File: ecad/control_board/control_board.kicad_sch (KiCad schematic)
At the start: 31 parts, among them J1 USB_C_Receptacle_USB2.0_16P, J2 JST SH, U1 W25Q16JVUXIQ, U2 NCP1117-3.3_SOT223, U3 RP2040, Y1 ABM8-272-T3

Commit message: [WIP]
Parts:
- removed U2: NCP1117-3.3_SOT223, Package_TO_SOT_SMD:SOT-223-3_TabPin2, symbol Regulator_Linear:NCP1117-3.3_SOT223
- added C17, C18: 100n, Capacitor_SMD:C_0402_1005Metric, symbol Device:C
- added J3, J4, J5: JST SH, Connector_JST:JST_SH_BM04B-SRSS-TB_1x04-1MP_P1.00mm_Vertical, symbol Connector_Generic:Conn_01x04
- added R10, R11, R8, R9: 5.1k, Resistor_SMD:R_0402_1005Metric, symbol Device:R
- added U2: TLV75733PDBV, Package_TO_SOT_SMD:SOT-23-5, symbol Regulator_Linear:TLV75733PDBV
- added U4: TCA9406DCTR, Package_SO:SSOP-8_2.95x2.8mm_P0.65mm, symbol Interface:TCA9406DC
- C4, C5: value 10u -> 2u2; footprint Capacitor_SMD:C_0805_2012Metric -> Capacitor_SMD:C_0402_1005Metric
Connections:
- net +3V3: now also C17.1, C18.1, J3.1 (Pin_1), J4.1 (Pin_1), J5.1 (Pin_1), R10.1, R11.1, R8.1, R9.1, U2.5 (OUT), U4.3 (VCCA), U4.7 (VCCB)
- net +5V: now also U2.1 (IN), U2.3 (EN)
- net GND: now also C17.2, C18.2, J3.4 (Pin_4), J4.4 (Pin_4), J5.4 (Pin_4), U2.2 (GND), U4.2 (GND)
- new net PICO/KEY/SCL: R8.2, U4.5 (SCL_A)
- new net PICO/KEY/SDA: R9.2, U4.4 (SDA_A)
- new net TOP/SCL: J3.3 (Pin_3), J4.3 (Pin_3), J5.3 (Pin_3), R10.2, U4.8 (SCL_B)
- new net TOP/SDA: J3.2 (Pin_2), J4.2 (Pin_2), J5.2 (Pin_2), R11.2, U4.1 (SDA_B)
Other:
- note added: "3V3 @ 1A LDO"
- note added: "Flash Memory"
- note added: "PUSH BUTTONS"
- note added: "USB Type C 2.0 RCPT"
- note added: "XTAL"
- moved on the sheet: BOOTSEL1, C1, C10, C11, C12, C13, C14, C15, C16, C2, C3, C4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

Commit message: Makes a control_board
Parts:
- added C19, C20, C21, C22: 100n, Capacitor_SMD:C_0402_1005Metric, symbol Device:C
- added J10, J11, J3, J4, J5, J9: JST SH 4, woodpecker:JST_SH_BM04B-SRSS-TB_1x04-1MP_P1.00mm_Vertical, symbol Connector_Generic:Conn_01x04
- added J12: JST PH 4, woodpecker:JST_PH_B4B-PH-SM4-TB_1x04-1MP_P2.00mm_Vertical, symbol Connector_Generic:Conn_01x04
- added J13, J14: JST PH 3, woodpecker:JST_PH_B3B-PH-SM4-TB_1x03-1MP_P2.00mm_Vertical, symbol Connector_Generic:Conn_01x03
- added R12, R13, R16, R17: 2.2k, Resistor_SMD:R_0402_1005Metric, symbol Device:R
- added R18, R19: 5.1k, Resistor_SMD:R_0402_1005Metric, symbol Device:R
- added U5, U6: TCA9406DCTR, Package_SO:SSOP-8_2.95x2.8mm_P0.65mm, symbol Interface:TCA9406DC
- J2: value JST SH -> JST SH 3; footprint Connector_JST:JST_SH_BM03B-SRSS-TB_1x03-1MP_P1.00mm_Vertical -> woodpecker:JST_SH_BM03B-SRSS-TB_1x03-1MP_P1.00mm_Vertical
- J6: renamed from J5; value JST SH -> JST SH 4; footprint Connector_JST:JST_SH_BM04B-SRSS-TB_1x04-1MP_P1.00mm_Vertical -> woodpecker:JST_SH_BM04B-SRSS-TB_1x04-1MP_P1.00mm_Vertical
- J7: renamed from J3; value JST SH -> JST SH 4; footprint Connector_JST:JST_SH_BM04B-SRSS-TB_1x04-1MP_P1.00mm_Vertical -> woodpecker:JST_SH_BM04B-SRSS-TB_1x04-1MP_P1.00mm_Vertical
- J8: renamed from J4; value JST SH -> JST SH 4; footprint Connector_JST:JST_SH_BM04B-SRSS-TB_1x04-1MP_P1.00mm_Vertical -> woodpecker:JST_SH_BM04B-SRSS-TB_1x04-1MP_P1.00mm_Vertical
- R10, R11: value 5.1k -> 2.2k
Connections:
- net PICO/KEY/SCL is gone; now on net I2C0/SCL: R8.2, U4.5 (SCL_A)
- net PICO/KEY/SDA is gone; now on net I2C0/SDA: R9.2, U4.4 (SDA_A)
- net +3V3: now also C19.1, C20.1, C21.1, C22.1, J10.1 (Pin_1), J11.1 (Pin_1), J3.1 (Pin_1), J4.1 (Pin_1), J5.1 (Pin_1), J9.1 (Pin_1), R12.1, R13.1, R16.1, R17.1, R18.1, R19.1, U5.3 (VCCA), U5.7 (VCCB), U6.3 (VCCA), U6.7 (VCCB)
- net +5V: now also J12.4 (Pin_4), J13.3 (Pin_3), J14.3 (Pin_3)
- net GND: now also C19.2, C20.2, C21.2, C22.2, J10.4 (Pin_4), J11.4 (Pin_4), J12.1 (Pin_1), J13.1 (Pin_1), J14.1 (Pin_1), J3.4 (Pin_4), J4.4 (Pin_4), J5.4 (Pin_4), J9.4 (Pin_4), U5.2 (GND), U6.2 (GND)
- net I2C0/SCL: now reaches U3.12 (GPIO9)
- net I2C0/SCL: now also U5.5 (SCL_A)
- net I2C0/SDA: now reaches U3.15 (GPIO12)
- net I2C0/SDA: now also U5.4 (SDA_A)
- net I2C_E: now reaches U3.2 (GPIO0)
- net I2C_E: now also U4.6 (OE), U5.6 (OE), U6.6 (OE)
- net BOT/DOUT: now reaches U3.30 (GPIO19)
- net BOT/DOUT: now also J14.2 (Pin_2)
- net MID/DOUT: now reaches U3.31 (GPIO20)
- net MID/DOUT: now also J13.2 (Pin_2)
- net TOP/DOUT: now reaches U3.39 (GPIO27_ADC1)
- net TOP/DOUT: now also J12.3 (Pin_3)
- net TOP/SDOUT: now reaches U3.40 (GPIO28_ADC2)
- net TOP/SDOUT: now also J12.2 (Pin_2)
- net I2C1/SCL: now reaches U3.5 (GPIO3)
- net I2C1/SCL: now also R18.2, U6.5 (SCL_A)
- net I2C1/SDA: now reaches U3.8 (GPIO6)
- net I2C1/SDA: now also R19.2, U6.4 (SDA_A)
- new net BOT/SCL: J10.3 (Pin_3), J11.3 (Pin_3), J9.3 (Pin_3), R12.2, U5.8 (SCL_B)
- new net BOT/SDA: J10.2 (Pin_2), J11.2 (Pin_2), J9.2 (Pin_2), R13.2, U5.1 (SDA_B)
- new net MID/SCL: J3.3 (Pin_3), J4.3 (Pin_3), J5.3 (Pin_3), R16.2, U6.8 (SCL_B)
- new net MID/SDA: J3.2 (Pin_2), J4.2 (Pin_2), J5.2 (Pin_2), R17.2, U6.1 (SDA_B)
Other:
- note added: "I2C Buffer Bot"
- note added: "I2C Buffer Mid"
- note added: "I2C Buffer Top"
- note added: "SWD"
- moved on the sheet: C10, C11, C12, C13, C14, C15, C16, C17, C18, C6, C7, C8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

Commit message: [WIP] Control board
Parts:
- removed C18, C19, C20, C21, C22: 100n, Capacitor_SMD:C_0402_1005Metric, symbol Device:C
- removed J10, J11, J3, J4, J5, J6, J7, J8, J9: JST SH 4, woodpecker:JST_SH_BM04B-SRSS-TB_1x04-1MP_P1.00mm_Vertical, symbol Connector_Generic:Conn_01x04
- removed J12: JST PH 4, woodpecker:JST_PH_B4B-PH-SM4-TB_1x04-1MP_P2.00mm_Vertical, symbol Connector_Generic:Conn_01x04
- removed J13, J14: JST PH 3, woodpecker:JST_PH_B3B-PH-SM4-TB_1x03-1MP_P2.00mm_Vertical, symbol Connector_Generic:Conn_01x03
- removed R10, R11, R12, R13, R16, R17: 2.2k, Resistor_SMD:R_0402_1005Metric, symbol Device:R
- removed R18, R19, R4, R8, R9: 5.1k, Resistor_SMD:R_0402_1005Metric, symbol Device:R
- removed R7: 200, Resistor_SMD:R_0402_1005Metric, symbol Device:R
- removed U4, U5, U6: TCA9406DCTR, Package_SO:SSOP-8_2.95x2.8mm_P0.65mm, symbol Interface:TCA9406DC
- added D1: 1N4148WS, Diode_SMD:D_SOD-323, symbol Diode:1N4148WS
- added FB1: FerriteBead, symbol Device:FerriteBead
- added U4: TUSB320I, Package_DFN_QFN:Texas_X2QFN-12_1.6x1.6mm_P0.4mm, symbol Interface_USB:TUSB320I
- C9: value 2u2 -> 1u; footprint Capacitor_SMD:C_0402_1005Metric -> (none)
- R3: value 5.1k -> 900k
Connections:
- net +3V3: no longer C17.1
- net +5V: no longer J1.A4 (VBUS), J1.A9 (VBUS), J1.B4 (VBUS), J1.B9 (VBUS)
- net CC1: now also U4.1 (CC1)
- net CC2: now also U4.2 (CC2); no longer R3.1
- net GND: now also U4.10 (GND), U4.11 (~{EN}), U4.3 (PORT); no longer R3.2
- net 3V3_ADC: no longer names the net of U3.43 (ADC_AVDD)
- net 3V3_ADC: no longer C9.1
- net BOT/DOUT: no longer names the net of U3.30 (GPIO19)
- net I2C0/SCL: no longer names the net of U3.12 (GPIO9)
- net I2C0/SDA: no longer names the net of U3.15 (GPIO12)
- net I2C1/SCL: no longer names the net of U3.5 (GPIO3)
- net I2C1/SDA: no longer names the net of U3.8 (GPIO6)
- net I2C_E: no longer names the net of U3.2 (GPIO0)
- net MID/DOUT: no longer names the net of U3.31 (GPIO20)
- net TOP/DOUT: no longer names the net of U3.39 (GPIO27_ADC1)
- net TOP/SDOUT: no longer names the net of U3.40 (GPIO28_ADC2)
- new net: R3.2, U4.4 (VBUS_DET)
- new net USB_OUT1: U4.7 (SDA/OUT1)
- new net USB_OUT2: U4.8 (SCL/OUT2)
- new net VBUS: D1.2 (A), FB1.2, R3.1
- new net VBUS_5V: C17.1, D1.1 (K), U4.12 (VDD)
- new net VBUS_UNFLT: C9.1, FB1.1, J1.A4 (VBUS), J1.A9 (VBUS), J1.B4 (VBUS), J1.B9 (VBUS)
- no-connect marks 2 -> 5
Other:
- note added: "USB CC Controller"
- note removed: "I2C Buffer Bot"
- note removed: "I2C Buffer Mid"
- note removed: "I2C Buffer Top"
- moved on the sheet: C10, C11, C12, C13, C14, C15, C16, C3, C4, C5, C6, C7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

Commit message: [WIP] control board
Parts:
- added C18, C19: 100n, Capacitor_SMD:C_0402_1005Metric, symbol Device:C
- added J10, J9: JST PH 3, woodpecker:JST_PH_S3B-PH-SM4-TB_1x03-1MP_P2.00mm_Horizontal, symbol Connector_Generic:Conn_01x03
- added J3, J4, J5, J6, J7, J8: JST SH 3, woodpecker:JST_SH_BM03B-SRSS-TB_1x03-1MP_P1.00mm_Vertical, symbol Connector_Generic:Conn_01x03
- added Q6: RE1C002UN, Package_TO_SOT_SMD:SOT-416, symbol Device:Q_NMOS_GSD
- added R4: 71k5, Resistor_SMD:R_0402_1005Metric, symbol Device:R
- added R7, R8: 27k, Resistor_SMD:R_0402_1005Metric, symbol Device:R
- added U5: TPS2552DRV, woodpecker:Texas_WSON-6-1EP_2x2mm_P0.65mm_EP1x1.6mm_ThermalVias, symbol woodpecker:TPS2552DRV
- J2: footprint woodpecker:JST_SH_BM03B-SRSS-TB_1x03-1MP_P1.00mm_Vertical -> woodpecker:JST_SH_SM03B-SRSS-TB_1x03-1MP_P1.00mm_Horizontal; MPN (none) -> SM03B-SRSS-TB
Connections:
- net +3V3: now also J3.1 (Pin_1), J4.1 (Pin_1), J5.1 (Pin_1), J6.1 (Pin_1), J7.1 (Pin_1), J8.1 (Pin_1)
- net +5V: now also J10.1 (Pin_1), J9.1 (Pin_1)
- net GND: now also C18.2, C19.2, J10.3 (Pin_3), J3.3 (Pin_3), J4.3 (Pin_3), J5.3 (Pin_3), J6.3 (Pin_3), J7.3 (Pin_3), J8.3 (Pin_3), J9.3 (Pin_3), Q6.2 (S), R4.2, R8.2, U5.4 (~{EN}), U5.5 (GND), U5.7 (PAD)
- net VBUS: now also C18.1, U5.6 (IN)
- new net: R4.1, R7.1, U5.2 (ILIM)
- new net: Q6.3 (D), R7.2
- new net +5V_LED: C19.1, U5.1 (OUT)
- new net LED_FULL_EN: Q6.1 (G), R8.1
- new net LED_OUT0: J9.2 (Pin_2)
- new net LED_OUT1: J10.2 (Pin_2)
- new net RX0: J8.2 (Pin_2)
- new net RX1: J3.2 (Pin_2)
- new net RX2: J4.2 (Pin_2)
- new net RX3: J5.2 (Pin_2)
- new net RX4: J6.2 (Pin_2)
- new net RX5: J7.2 (Pin_2)
- new net ~{LED_FAULT}: U5.3 (~{FAULT})
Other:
- note added: "LED Current Limited Switch 330ma/1.2A"
- moved on the sheet: C10, C11, C12, C13, C14, C15, C16, C4, C5, C6, C7, C8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

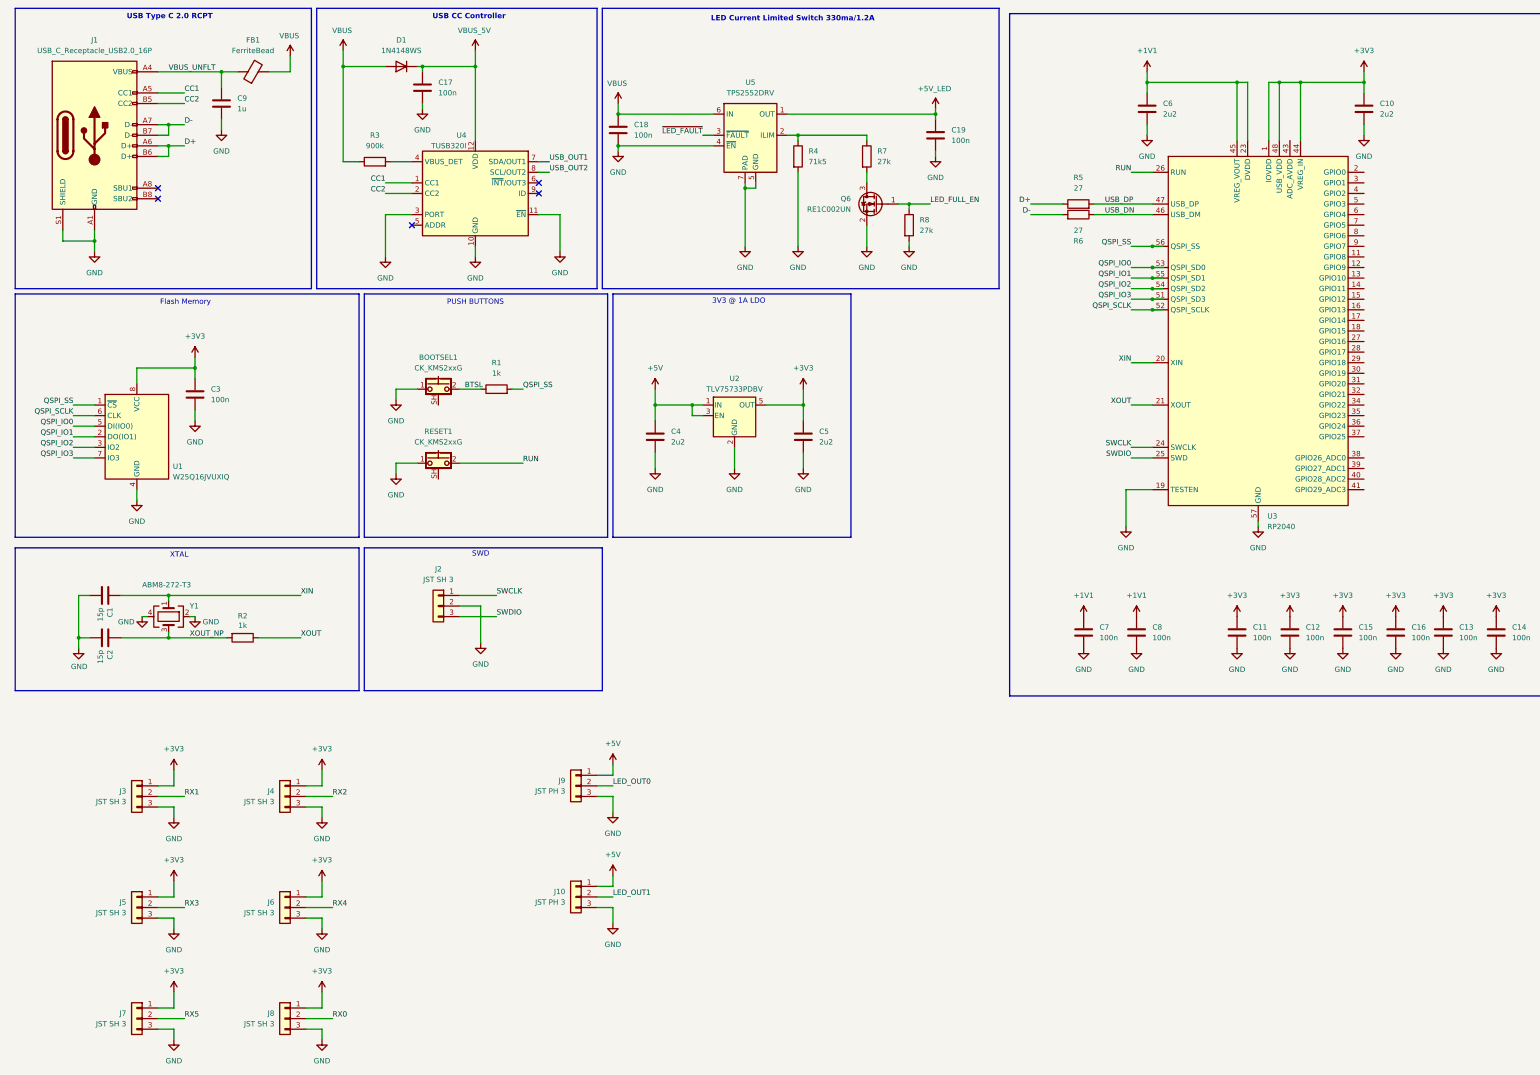
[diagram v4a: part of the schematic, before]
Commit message: Layouted new control board
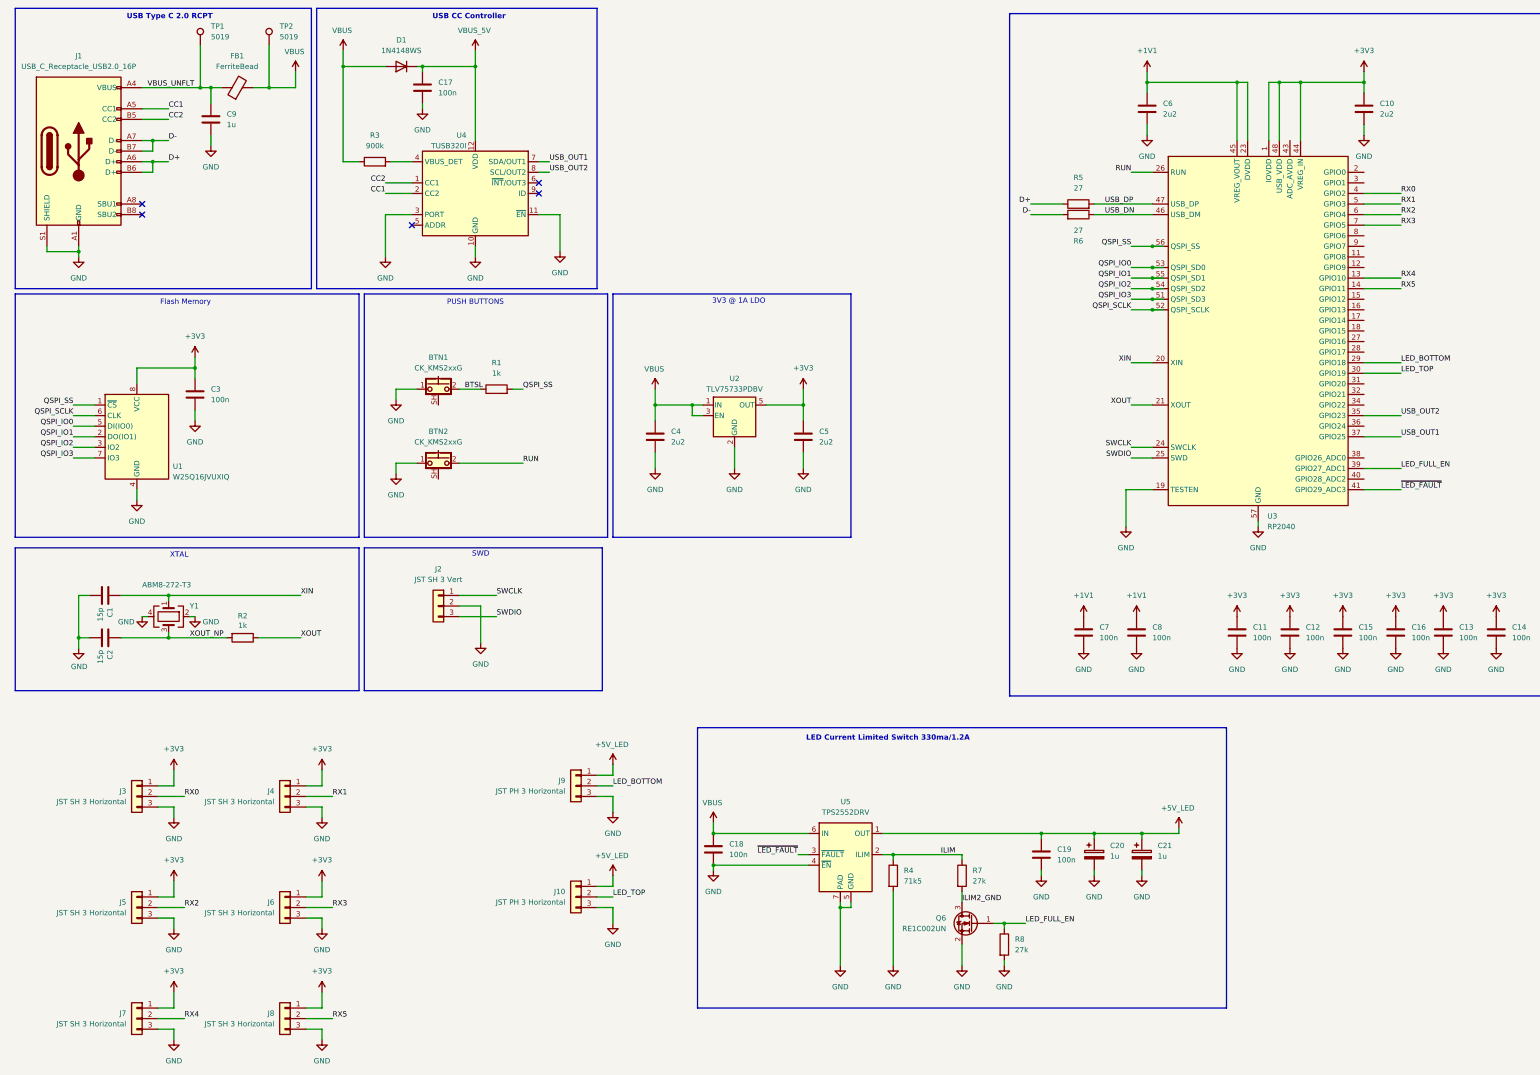
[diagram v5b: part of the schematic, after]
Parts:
- added C20, C21: 1u, Capacitor_SMD:CP_Elec_8x10.5, symbol Device:C_Polarized
- added TP1, TP2: 5019, TestPoint:TestPoint_Keystone_5019_Miniature, symbol Connector:TestPoint
- BTN1: renamed from BOOTSEL1; footprint Button_Switch_SMD:SW_SPST_CK_KMS2xxGP -> woodpecker:SW_SPST_CK_KMS2xxGP
- BTN2: renamed from RESET1; footprint Button_Switch_SMD:SW_SPST_CK_KMS2xxGP -> woodpecker:SW_SPST_CK_KMS2xxGP
- C4, C5: footprint Capacitor_SMD:C_0402_1005Metric -> Capacitor_SMD:C_0603_1608Metric
- FB1: footprint (none) -> Resistor_SMD:R_1206_3216Metric; MPN (none) -> HCB 3216KF-501T30
- J10, J9: value JST PH 3 -> JST PH 3 Horizontal; MPN B3B-PH-SM4-TB -> S3B-PH-SM4-TB
- J2: value JST SH 3 -> JST SH 3 Vert; footprint woodpecker:JST_SH_SM03B-SRSS-TB_1x03-1MP_P1.00mm_Horizontal -> woodpecker:JST_SH_BM03B-SRSS-TB_1x03-1MP_P1.00mm_Vertical; MPN SM03B-SRSS-TB -> BM03B-SRSS-TB
- J3, J4, J5, J6, J7, J8: value JST SH 3 -> JST SH 3 Horizontal; footprint woodpecker:JST_SH_BM03B-SRSS-TB_1x03-1MP_P1.00mm_Vertical -> woodpecker:JST_SH_SM03B-SRSS-TB_1x03-1MP_P1.00mm_Horizontal; MPN BM03B-SRSS-TB -> SM03B-SRSS-TB
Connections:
- net LED_OUT0 is gone; now on net LED_BOTTOM: J9.2 (Pin_2)
- net LED_OUT1 is gone; now on net LED_TOP: J10.2 (Pin_2)
- net +5V_LED: now also J10.1 (Pin_1), J9.1 (Pin_1), C20.1, C21.1
- net CC1: now also U4.2 (CC2); no longer U4.1 (CC1)
- net CC2: now also U4.1 (CC1); no longer U4.2 (CC2)
- net GND: now also C20.2, C21.2
- net LED_FULL_EN: now also U3.39 (GPIO27_ADC1)
- net RX0: now also J3.2 (Pin_2), U3.4 (GPIO2); no longer J8.2 (Pin_2)
- net RX1: now also J4.2 (Pin_2), U3.5 (GPIO3); no longer J3.2 (Pin_2)
- net RX2: now also J5.2 (Pin_2), U3.6 (GPIO4); no longer J4.2 (Pin_2)
- net RX3: now also J6.2 (Pin_2), U3.7 (GPIO5); no longer J5.2 (Pin_2)
- net RX4: now also J7.2 (Pin_2), U3.13 (GPIO10); no longer J6.2 (Pin_2)
- net RX5: now also J8.2 (Pin_2), U3.14 (GPIO11); no longer J7.2 (Pin_2)
- net USB_OUT1: now also U3.37 (GPIO25)
- net USB_OUT2: now also U3.35 (GPIO23)
- net VBUS: now also C4.1, U2.1 (IN), U2.3 (EN), TP2.1
- net VBUS_UNFLT: now also TP1.1
- net ~{LED_FAULT}: now also U3.41 (GPIO29_ADC3)
- net ILIM: now reaches R4.1, R7.1, U5.2 (ILIM)
- net ILIM2_GND: now reaches Q6.3 (D), R7.2
- net LED_BOTTOM: now reaches U3.29 (GPIO18)
- net LED_TOP: now reaches U3.30 (GPIO19)
- removed net +5V: C4.1, J10.1 (Pin_1), J9.1 (Pin_1), U2.1 (IN), U2.3 (EN)
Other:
- moved on the sheet: C18, C19, C9, FB1, J1, Q6, R4, R7, R8, U5

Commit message: Adds a first logo
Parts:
- BTN1, BTN2: MPN (none) -> KMS231GP LFS
- C1, C2: MPN (none) -> GCM1555C1H150JA16D
- C10, C6: MPN (none) -> GRM155Z71A225KE01D
- C11, C12, C13, C14, C15, C16, C17, C18, C19, C3, C7, C8: MPN (none) -> CL05B104KP5NNNC
- C20, C21: value 1u -> 1000u; MPN (none) -> EEE-FT1A102GP
- C4, C5: MPN (none) -> CL10B225KP8NNNC
- C9: footprint (none) -> Capacitor_SMD:C_0603_1608Metric; MPN (none) -> CL10B105KP8NNNC
- D1: MPN (none) -> 1N4148WS
- J1: MPN (none) -> USB4105-GF-A
- R1, R2: MPN (none) -> RC0402FR-071KL
- R3: value 900k -> 910k; MPN (none) -> RC0402FR-07910KL
- R4: MPN (none) -> RC0402FR-1371K5L
- R5, R6: MPN (none) -> RC0402FR-0727RL
- R7, R8: MPN (none) -> RC0402FR-0727KL
- TP1, TP2: MPN (none) -> 5019
- U1: MPN (none) -> W25Q16JVUXIQ TR
- U3: MPN (none) -> RP2040
- U5: MPN (none) -> TPS2552DRVR
- Y1: MPN (none) -> ABM8-272-T3
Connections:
- no-connect marks 5 -> 24
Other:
- note added: "Daughter Board Input"
- note added: "RP2040 MCU"
- note added: "WS2812 LED Output"
- moved on the sheet: C1, C10, C11, C12, C13, C14, C15, C16, C18, C19, C2, C20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

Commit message: Updated Controller for I2C controlled LED Matrices
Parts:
- removed C20, C21: 1000u, Capacitor_SMD:CP_Elec_8x10.5, symbol Device:C_Polarized
- removed J10, J9: JST PH 3 Horizontal, woodpecker:JST_PH_S3B-PH-SM4-TB_1x03-1MP_P2.00mm_Horizontal, symbol Connector_Generic:Conn_01x03
- removed J3, J4, J5, J6, J7, J8: JST SH 3 Horizontal, woodpecker:JST_SH_SM03B-SRSS-TB_1x03-1MP_P1.00mm_Horizontal, symbol Connector_Generic:Conn_01x03
- added C20, C21, C22, C23: 100n, Capacitor_SMD:C_0603_1608Metric, symbol Device:C
- added J3, J4, J5, J6, J7, J8: JST SH 6P, Connector_JST:JST_SH_SM06B-SRSS-TB_1x06-1MP_P1.00mm_Horizontal, symbol Connector_Generic:Conn_01x06
- added R10, R13, R14, R9: 2.2k, Resistor_SMD:R_0603_1608Metric, symbol Device:R
- added R11, R12, R15, R16: 3.3k, Resistor_SMD:R_0603_1608Metric, symbol Device:R
- added U6, U7: TCA9406DCTR, Package_SO:SSOP-8_2.95x2.8mm_P0.65mm, symbol Interface:TCA9406DC
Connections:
- net +3V3: now also C20.1, C21.1, C22.1, C23.1, J3.2 (Pin_2), J4.2 (Pin_2), J5.2 (Pin_2), J6.2 (Pin_2), J7.2 (Pin_2), J8.2 (Pin_2), R10.1, R11.1, R12.1, R13.1, R14.1, R15.1, R16.1, R9.1, U6.3 (VCCA), U6.6 (OE), U6.7 (VCCB), U7.3 (VCCA), U7.6 (OE), U7.7 (VCCB)
- net +5V_LED: now also J3.1 (Pin_1), J4.1 (Pin_1), J5.1 (Pin_1), J6.1 (Pin_1), J7.1 (Pin_1), J8.1 (Pin_1)
- net GND: now also C20.2, C21.2, C22.2, C23.2, J3.6 (Pin_6), J4.6 (Pin_6), J5.6 (Pin_6), J6.6 (Pin_6), J7.6 (Pin_6), J8.6 (Pin_6), U6.2 (GND), U7.2 (GND)
- net LED_FULL_EN: now also U3.40 (GPIO28_ADC2); no longer U3.39 (GPIO27_ADC1)
- net RX0: now also J3.5 (Pin_5)
- net RX1: now also J4.5 (Pin_5)
- net RX2: now also J5.5 (Pin_5)
- net RX3: now also U3.35 (GPIO23), J6.5 (Pin_5); no longer U3.7 (GPIO5)
- net RX4: now also U3.36 (GPIO24), J7.5 (Pin_5); no longer U3.13 (GPIO10)
- net RX5: now also U3.37 (GPIO25), J8.5 (Pin_5); no longer U3.14 (GPIO11)
- net USB_OUT1: now also U3.39 (GPIO27_ADC1); no longer U3.37 (GPIO25)
- net USB_OUT2: now also U3.38 (GPIO26_ADC0); no longer U3.35 (GPIO23)
- net RP_SCL0: now reaches U3.12 (GPIO9)
- net RP_SCL0: now also R11.2, U6.5 (SCL_A)
- net RP_SDA0: now reaches U3.15 (GPIO12)
- net RP_SDA0: now also R12.2, U6.4 (SDA_A)
- net RP_SDA1: now reaches U3.34 (GPIO22)
- net RP_SDA1: now also R16.2, U7.4 (SDA_A)
- net LED_BOTTOM: no longer names the net of U3.29 (GPIO18)
- net LED_TOP renamed RP_SCL1
- net RP_SCL1: now also R15.2, U7.5 (SCL_A)
- new net SCL0: J3.4 (Pin_4), J4.4 (Pin_4), J5.4 (Pin_4), R9.2, U6.8 (SCL_B)
- new net SCL1: J6.4 (Pin_4), J7.4 (Pin_4), J8.4 (Pin_4), R13.2, U7.8 (SCL_B)
- new net SDA0: J3.3 (Pin_3), J4.3 (Pin_3), J5.3 (Pin_3), R10.2, U6.1 (SDA_B)
- new net SDA1: J6.3 (Pin_3), J7.3 (Pin_3), J8.3 (Pin_3), R14.2, U7.1 (SDA_B)
- no-connect marks 24 -> 21
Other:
- note removed: "WS2812 LED Output"
